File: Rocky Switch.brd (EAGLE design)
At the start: 68.4 x 47 mm, 27 parts, among them T1 2SC1815, T2 2SC1815, T3 C1815

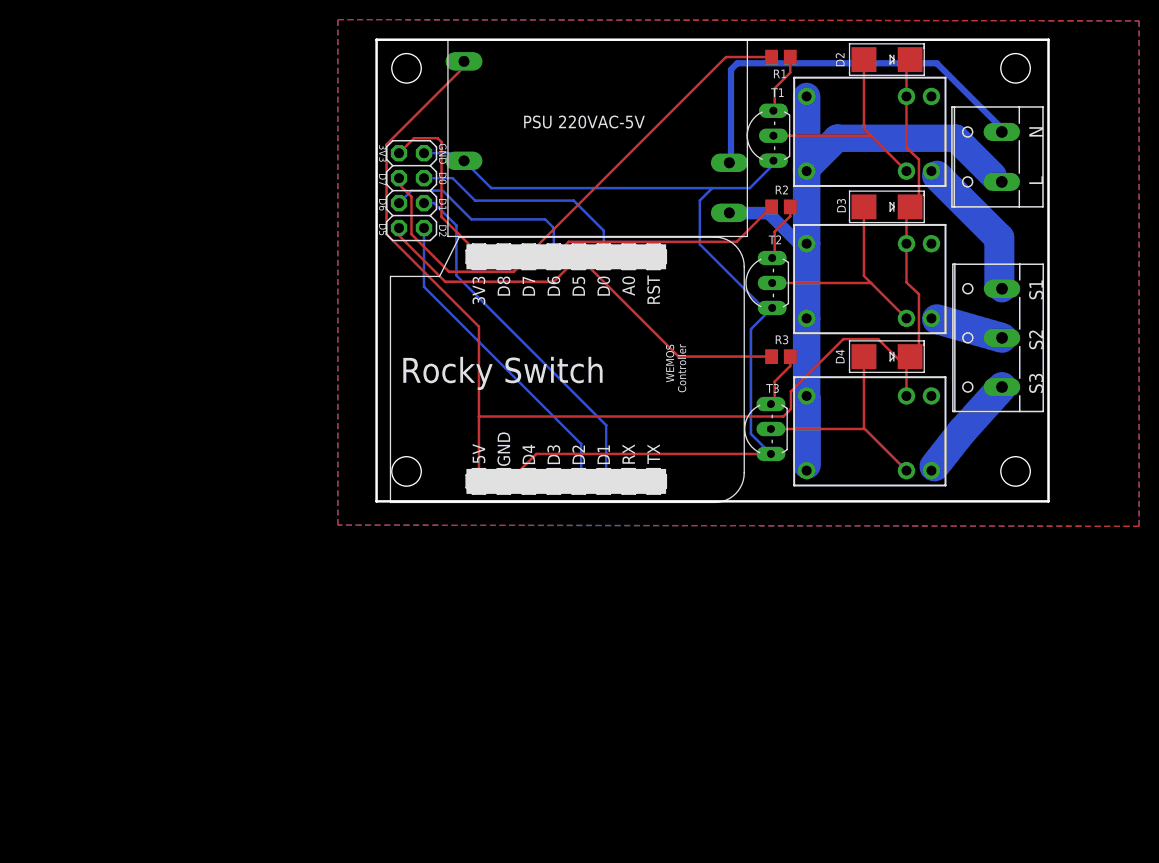
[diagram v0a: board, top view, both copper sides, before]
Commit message: Update to new version to back to use SSR instead of mechanical relays
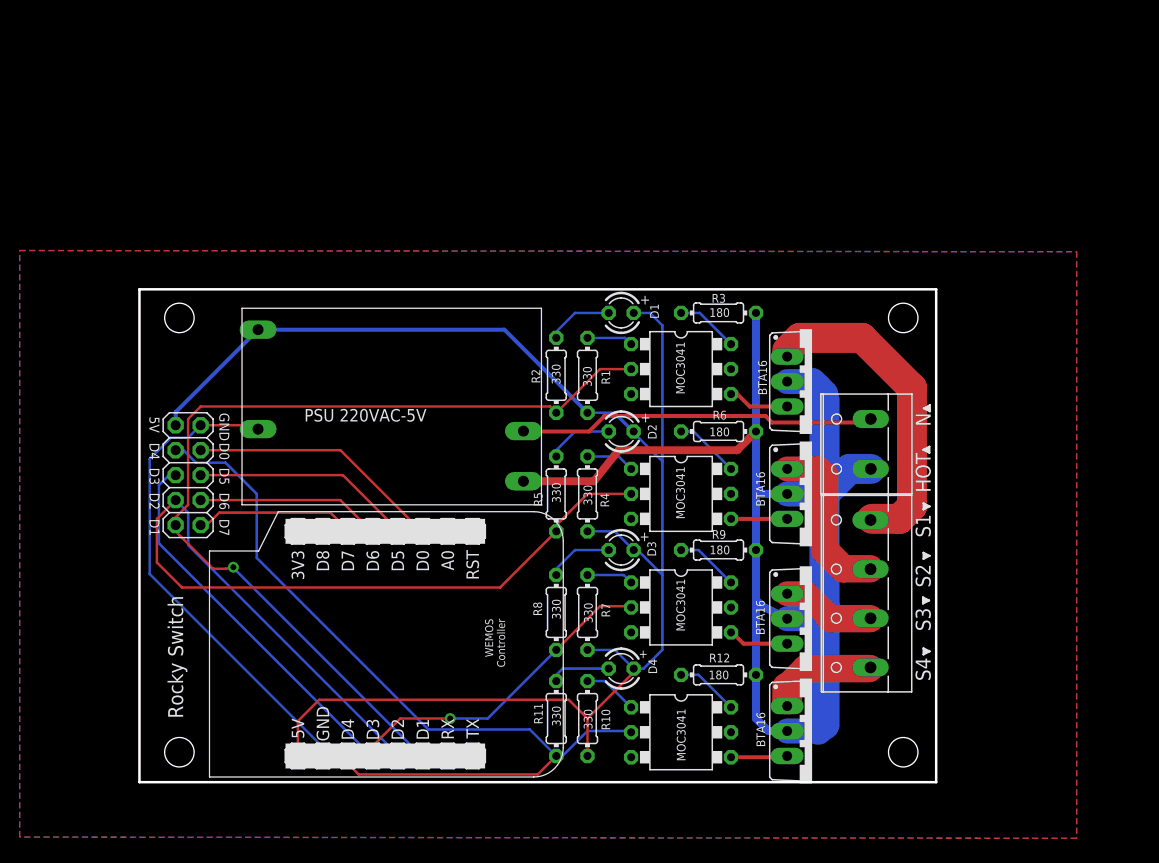
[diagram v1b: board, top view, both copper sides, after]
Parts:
- removed JP2: (no value), adafruit:2X04
- removed OUT1: (no value), con-wago-500:W237-103
- removed U$3, U$4, U$5: MINIATURE_RELAY_JRC_21F, My Eagle Lib:MINIATURE_RELAY_JRC_21F
- added D1: (no value), led:LED3MM
- added JP1: (no value), pinhead:2X05
- added OK1, OK2, OK3, OK4: MOC3041, optocoupler:DIL06B
- added R10, R11, R4, R5, R7, R8: 330, rcl:0204/7
- added R12, R6, R9: 180, rcl:0204/7
- added T4: BTA16, triac:TO220BV
- added U$2: (no value), dicons:ICON_PIN1_B
- added X1: (no value), con-wago-500:W237-4
- D2, D3, D4: device adafruit:SMADIODE -> led:LED3MM
- R1, R2: value 1K -> 330; device rcl:R0805 -> rcl:0204/7
- R3: value 1K -> 180; device rcl:R0805 -> rcl:0204/7
- T1, T2: value 2SC1815 -> BTA16; device transistor:TO92-ECB -> triac:TO220BV
- T3: value C1815 -> BTA16; device transistor:TO92-ECB -> triac:TO220BV
- moved U$17 63.6 mm to (37.5, 16.5), turned to 0 degrees
- moved D2 46.5 mm to (49.8, 39.4)
- moved D3 44.2 mm to (49.8, 27.3)
- moved D4 41.7 mm to (49.8, 15.2)
- moved R1 37.9 mm to (46.4, 45.1), turned to 90 degrees
- moved U$6 36.8 mm to (4.83, 6.73)
- moved U$1 34.4 mm to (26.0, 41.9)
- moved U$9 34.3 mm to (4.83, 50.9)
- moved U$10 33.5 mm to (16.9, 29.2)
- moved AC 32.1 mm to (74.5, 38.1)
- moved U$11 30.8 mm to (80.6, 41.7), flipped to the top, turned to 0 degrees
- moved U$7 30.8 mm to (78.5, 6.73)
- moved U$12 30.0 mm to (80.5, 37.5), flipped to the top, turned to 0 degrees
- moved R2 28.6 mm to (43.2, 45.1), turned to 270 degrees
- moved U$8 27.9 mm to (78.5, 50.9)
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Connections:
- removed net N$1: D2.A, T1.C, U$3.COIL2
- removed net N$11: OUT1.1, U$5.NO
- removed net N$12: OUT1.2, U$4.NO
- removed net N$3: D3.A, T2.C, U$4.COIL2
- removed net N$4: D4.A, T3.C, U$5.COIL2
- removed net N$5: R3.2, T3.B
- removed net N$6: R2.2, T2.B
- removed net N$7: R1.2, T1.B
- removed net N$8: OUT1.3, U$3.NO
- new net N$10: OK1.1, R1.2
- new net N$14: OK1.6, R3.1
- new net N$15: OK2.4, T2.G
- new net N$16: OK2.1, R4.2
- new net N$17: OK2.6, R6.1
- new net N$18: OK3.4, T3.G
- new net N$19: OK3.1, R7.2
- new net N$20: OK3.6, R9.1
- new net N$21: T3.T1, X1.2
- new net N$22: T2.T1, X1.3
- new net N$23: T1.T1, X1.4
- new net N$28: D1.K, R2.1
- new net N$29: D2.K, R5.1
- new net N$30: D3.K, R8.1
- new net N$32: OK4.4, T4.G
- new net N$33: OK4.1, R10.2
- new net N$34: OK4.6, R12.1
- new net N$35: T4.T1, X1.1
- new net N$38: D4.K, R11.1
- new net N$9: OK1.4, T1.G
- net 3V3: no longer JP2.1
- net 5V: now also D1.A, D2.A, D3.A, D4.A, JP1.10, R1.1, R10.1, R4.1, R7.1; no longer D2.C, D3.C, D4.C, U$3.COIL1, U$4.COIL1, U$5.COIL1
- net AC_L: now also R12.2, R3.2, R6.2, R9.2, T1.T2, T2.T2, T3.T2, T4.T2; no longer U$3.COM1, U$3.COM2, U$4.COM1, U$4.COM2, U$5.COM1, U$5.COM2
- net D0: now also JP1.7; no longer JP2.4
- net D1: now also JP1.2, OK1.2, R2.2; no longer JP2.6
- net D2: now also JP1.4, OK2.2, R5.2; no longer JP2.8
- net D3: now also JP1.6, OK3.2, R8.2
- net D4: now also JP1.8, OK4.2, R11.2
- net D5: now also JP1.5; no longer JP2.7, R3.1
- net D6: now also JP1.3; no longer JP2.5, R2.1
- net D7: now also JP1.1; no longer JP2.3, R1.1
- net GND: now also JP1.9; no longer JP2.2, T1.E, T2.E, T3.E
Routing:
- net D4: track 0.00 -> 87.5 mm
- net AC_L: track 71.0 -> 154.6 mm
- net D3: track 0.00 -> 72.2 mm, vias 0 -> 1
- net D2: track 32.4 -> 96.0 mm
- net D1: track 36.8 -> 94.5 mm, vias 0 -> 1
- net GND: track 99.8 -> 50.3 mm
- net D7: track 53.7 -> 16.2 mm
- net N$23: track 0.00 -> 32.2 mm
- net 5V: track 135.9 -> 163.9 mm
- net D6: track 45.3 -> 18.9 mm
- net D5: track 46.0 -> 22.4 mm
- net N$3: track 23.2 -> 0.00 mm
- net N$1: track 23.1 -> 0.00 mm
- net N$4: track 23.0 -> 0.00 mm
- net 3V3: track 18.2 -> 0.00 mm
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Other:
- board size 68.4 x 47 mm -> 81.1 x 50.2 mm
- board text added: "+"
- board text added: "5V"
- board text added: "D3"
- board text added: "D4"
- board text added: "HOT"
- board text added: "S4"
- board text removed: "3V3"
- board text removed: "L"

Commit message: Update board design to version 0.2
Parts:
- removed OK1, OK2, OK3, OK4: MOC3041, optocoupler:DIL06B
- added U1, U2, U3, U4: MOC3041, SparkFun-DiscreteSemi:DIL06
- D1: value (none) -> Relay1; device led:LED3MM -> adafruit:CHIP-LED0805
- D2: value (none) -> Relay2; device led:LED3MM -> adafruit:CHIP-LED0805
- D3: value (none) -> Relay3; device led:LED3MM -> adafruit:CHIP-LED0805
- D4: value (none) -> Relay4; device led:LED3MM -> adafruit:CHIP-LED0805
- R1, R10, R11, R12, R2, R3, R4, R5, R6, R7, R8, R9: device rcl:0204/7 -> rcl:R0805
- moved D1 50.0 mm to (9.27, 22.1), turned to 270 degrees
- moved D2 45.4 mm to (9.27, 18.8), turned to 270 degrees
- moved D3 42.2 mm to (9.27, 15.5), turned to 270 degrees
- moved D4 40.6 mm to (9.27, 12.2), turned to 270 degrees
- moved R3 35.0 mm to (38.7, 23.4)
- moved R6 29.4 mm to (38.7, 18.8)
- moved R2 29.3 mm to (23.5, 23.4), turned to 0 degrees
- moved R1 26.5 mm to (31.1, 23.4), turned to 0 degrees
- moved R9 24.3 mm to (38.7, 15.0)
- moved R5 24.3 mm to (23.5, 18.8), turned to 180 degrees
- moved U$17 21.3 mm to (27.9, 35.6), flipped to the top
- moved R12 21.2 mm to (38.7, 11.2)
- moved R4 20.8 mm to (31.1, 18.8), turned to 0 degrees
- moved R8 20.6 mm to (23.5, 15.0), turned to 0 degrees
- moved R11 19.7 mm to (23.5, 11.2), turned to 0 degrees
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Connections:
- net D1: now also U1.2; no longer OK1.2
- net D2: now also U2.2; no longer OK2.2
- net D3: now also U3.2; no longer OK3.2
- net D4: now also U4.2; no longer OK4.2
- net N$10: now also U1.1; no longer OK1.1
- net N$14: now also U1.6; no longer OK1.6
- net N$15: now also U2.4; no longer OK2.4
- net N$16: now also U2.1; no longer OK2.1
- net N$17: now also U2.6; no longer OK2.6
- net N$18: now also U3.4; no longer OK3.4
- net N$19: now also U3.1; no longer OK3.1
- net N$20: now also U3.6; no longer OK3.6
- net N$28: now also D1.C; no longer D1.K
- net N$29: now also D2.C; no longer D2.K
- net N$30: now also D3.C; no longer D3.K
- net N$32: now also U4.4; no longer OK4.4
- net N$33: now also U4.1; no longer OK4.1
- net N$34: now also U4.6; no longer OK4.6
- net N$38: now also D4.C; no longer D4.K
- net N$9: now also U1.4; no longer OK1.4
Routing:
- net 5V: track 163.9 -> 83.0 mm, vias 0 -> 1
- net AC_L: track 154.6 -> 104.9 mm
- net N$10: track 4.71 -> 52.0 mm, vias 0 -> 1
- net N$14: track 6.40 -> 53.6 mm, vias 0 -> 2
- net D2: track 96.0 -> 74.5 mm, vias 0 -> 2
- net N$17: track 6.66 -> 24.5 mm, vias 0 -> 1
- net D4: track 87.5 -> 71.9 mm, vias 0 -> 3
- net N$16: track 4.97 -> 20.0 mm, vias 0 -> 1
- net N$20: track 6.45 -> 20.4 mm, vias 0 -> 1
- net N$34: track 6.45 -> 19.7 mm
- net N$19: track 4.76 -> 16.8 mm, vias 0 -> 1
- net AC_N: track 36.4 -> 25.3 mm
- net D1: track 94.5 -> 84.5 mm
- net N$29: track 6.76 -> 16.0 mm
- net N$33: track 5.55 -> 13.6 mm, vias 0 -> 1
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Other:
- board size 81.1 x 50.2 mm -> 69.6 x 47.6 mm
- board text added: "Rocky Switch v0.2"
- board text removed: "+"
- board text removed: "Rocky Switch"

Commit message: Update design to version 0.3
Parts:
- R12, R3, R6, R9: device rcl:R0805 -> rcl:0204/7
- moved R3 28.9 mm to (49.7, 50.1)
- moved R6 20.4 mm to (49.5, 36.1)
- moved R9 14.7 mm to (49.8, 24.6)
- moved R12 11.2 mm to (49.6, 13.8)
- moved U4 1.42 mm to (48.3, 7.62)
- moved U1 0.90 mm to (48.3, 43.8)
- moved U3 0.90 mm to (48.3, 18.4)
- moved U2 0.64 mm to (48.3, 29.8)
- moved JP1 0.63 mm to (7.62, 38.1)
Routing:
- net N$14: track 53.6 -> 7.35 mm, vias 2 -> 0
- net N$17: track 24.5 -> 7.48 mm, vias 1 -> 0
- net N$20: track 20.4 -> 7.21 mm, vias 1 -> 0
- net N$34: track 19.7 -> 7.40 mm
- net D1: track 84.5 -> 79.8 mm, vias 1 -> 3
- net D4: track 71.9 -> 69.8 mm
- net GND: track 48.2 -> 46.2 mm, vias 0 -> 1
- net N$10: track 52.0 -> 50.2 mm
- net N$19: track 16.8 -> 15.3 mm, vias 1 -> 0
- net N$9: track 4.57 -> 5.89 mm
- net N$32: track 4.57 -> 5.73 mm
- net N$33: track 13.6 -> 12.5 mm
- net N$18: track 5.10 -> 5.99 mm
- net D7: track 19.7 -> 19.0 mm
- net D6: track 23.4 -> 22.8 mm
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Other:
- board text added: "Rocky Switch v0.3"
- board text removed: "Rocky Switch v0.2"

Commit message: Update design to version 1.0
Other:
- board text added: "Rocky Switch v1.0"
- board text removed: "Rocky Switch v0.3"
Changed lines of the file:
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@@
 <text x="18.796" y="45.466" size="1.27" layer="25" font="vector" ratio="15">PSU 220VAC-5V</text>
 <text x="14.351" y="41.021" size="2.413" layer="25" font="vector" ratio="15">HIGH VOLTAGE</text>
-<text x="4.318" y="30.48" size="1.397" layer="25" font="vector" ratio="20" rot="SR270">Rocky Switch v0.3</text>
+<text x="4.318" y="30.48" size="1.397" layer="25" font="vector" ratio="20" rot="SR270">Rocky Switch v1.0</text>
 <text x="71.755" y="33.147" size="1.524" layer="25" font="vector" ratio="20" rot="SR90">HOT</text>
 <text x="71.755" y="39.878" size="1.524" layer="25" font="vector" ratio="20" rot="R90">N</text>
